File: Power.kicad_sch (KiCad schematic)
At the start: 56 parts, among them J2 Charge, J3 Battery, Q1 AO3401A, Q2 AO3400A, Q3 AO3401A, U4 FUSB303BTMX, U5 TPS61089, U6 D3V3XA4B10LP, U7 BQ25895RTW, U8 TPS63001

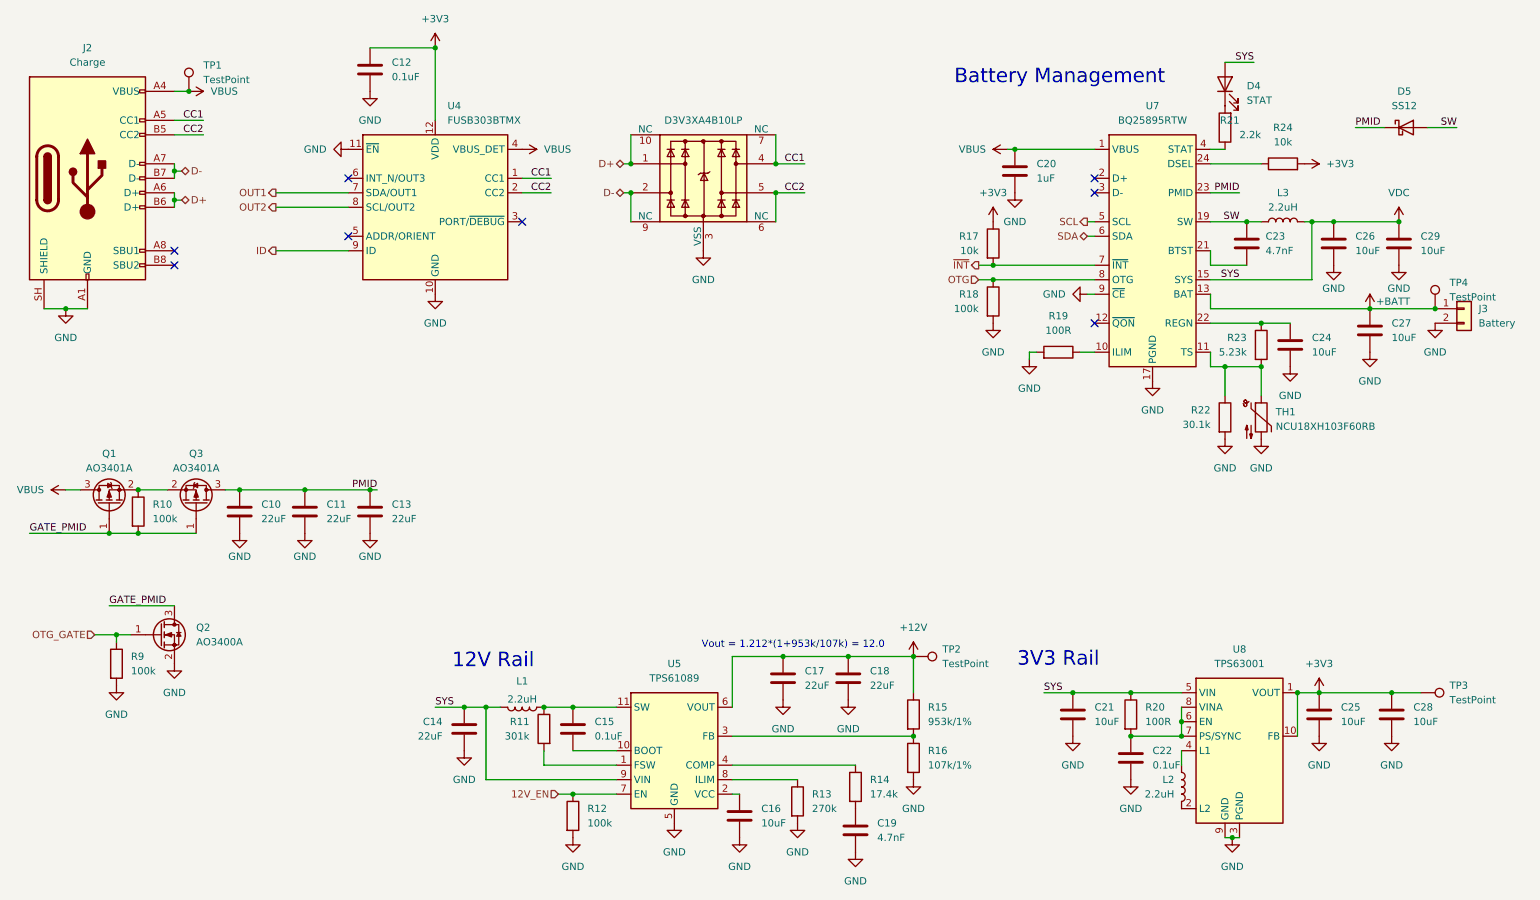
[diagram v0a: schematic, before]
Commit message: Finalize routed Cryobelt PCB for fabrication
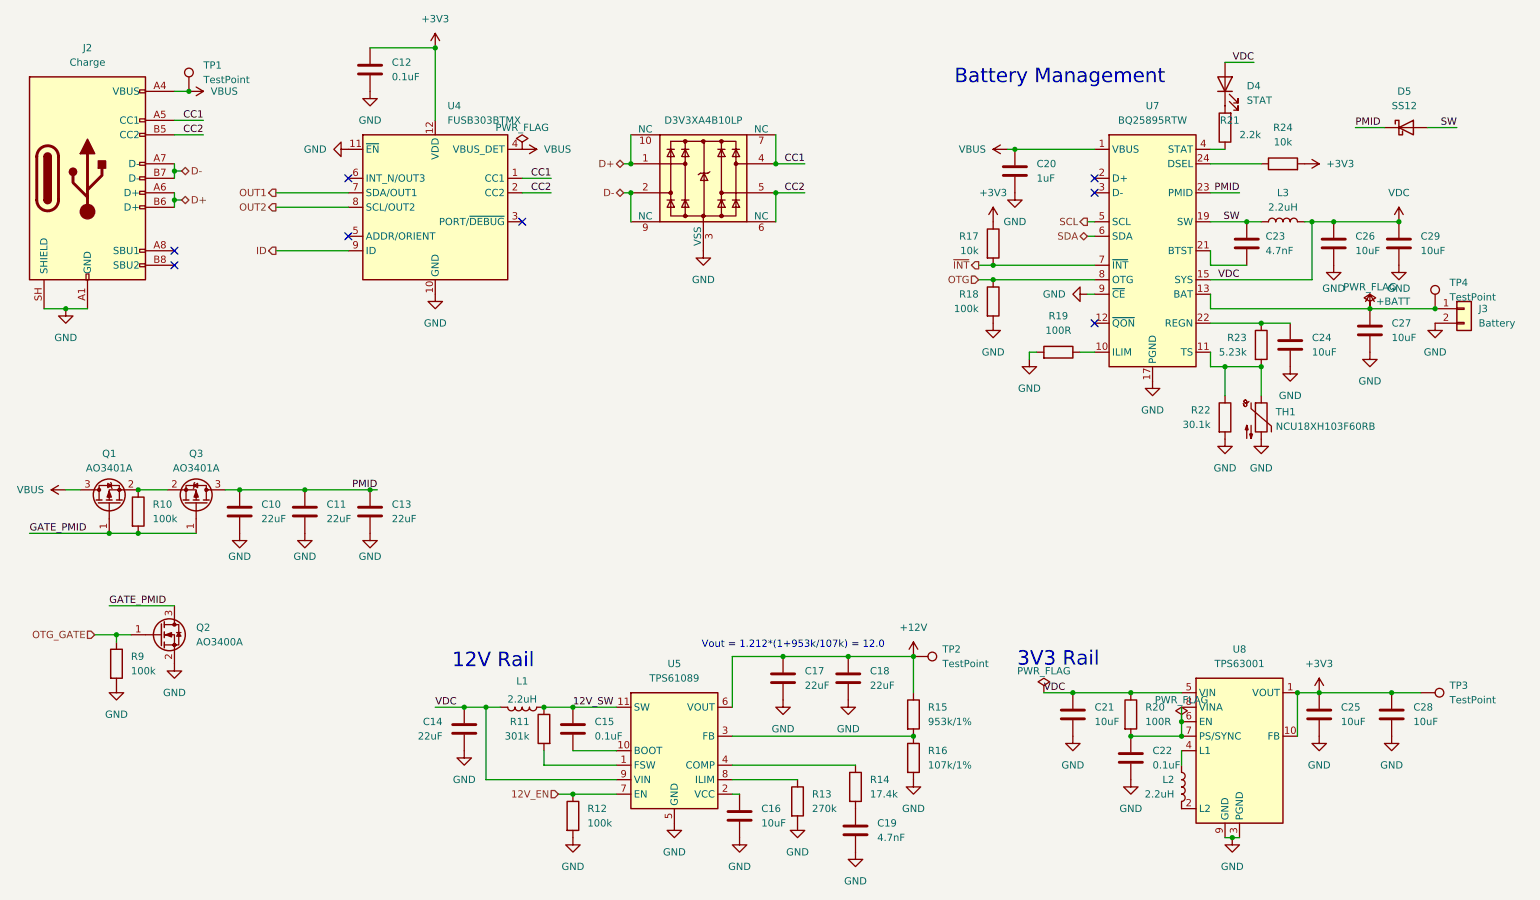
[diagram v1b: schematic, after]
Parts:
- C10, C11, C13, C17, C18: footprint Capacitor_SMD:C_0603_1608Metric -> Capacitor_SMD:C_0805_2012Metric; LCSC Part # (none) -> C20416420; MPN (none) -> TCC0805X5R226M250FT; Manufacturer (none) -> CCTC
- C12, C15, C22: LCSC Part # (none) -> C14663; MPN (none) -> CC0603KRX7R9BB104; Manufacturer (none) -> YAGEO
- C14: LCSC Part # (none) -> C86295; MPN (none) -> CL10A226MP8NUNE; Manufacturer (none) -> Samsung Electro-Mechanics
- C16, C21, C24, C25, C26, C27, C28, C29: LCSC Part # (none) -> C703114; MPN (none) -> GRM188R61A106KAALD; Manufacturer (none) -> Murata
- C19, C23: LCSC Part # (none) -> C106218; MPN (none) -> CC0603KRX7R9BB472; Manufacturer (none) -> YAGEO
- C20: LCSC Part # (none) -> C86012; MPN (none) -> GRM188R61A105KA61D; Manufacturer (none) -> Murata
- D4: LCSC Part # (none) -> C2286; MPN (none) -> KT-0603R; Manufacturer (none) -> Hubei KENTO Elec
- D5: LCSC Part # (none) -> C184027; MPN (none) -> SS12; Manufacturer (none) -> onsemi
- J2: LCSC Part # (none) -> C5143397; MPN (none) -> USB4110-GF-A; Manufacturer (none) -> Global Connector Technology
- J3: footprint Connector_Wire:SolderWire-0.5sqmm_1x02_P4.6mm_D0.9mm_OD2.1mm -> Connector_JST:JST_PH_S2B-PH-K_1x02_P2.00mm_Horizontal; LCSC Part # (none) -> C173752; MPN (none) -> S2B-PH-K-S(LF)(SN); Manufacturer (none) -> JST
- L1, L3: footprint Inductor_SMD:L_APV_ANR4020 -> Cryobelt:FEXU0420; LCSC Part # (none) -> C54777963; MPN (none) -> FEXU0420S2R2MBS; Manufacturer (none) -> cjiang
- L2: LCSC Part # (none) -> C135262; MPN (none) -> SMNR4020-2.2UH; Manufacturer (none) -> Shun Xiang Nuo
- Q1, Q3: LCSC Part # (none) -> C15127; MPN (none) -> AO3401A; Manufacturer (none) -> Alpha & Omega Semiconductor
- Q2: LCSC Part # (none) -> C20917; MPN (none) -> AO3400A; Manufacturer (none) -> Alpha & Omega Semiconductor
- R10, R12, R9: LCSC Part # (none) -> C14675; MPN (none) -> RC0603FR-07100KL; Manufacturer (none) -> YAGEO
- R11: LCSC Part # (none) -> C273742; MPN (none) -> RC0603FR-07301KL; Manufacturer (none) -> YAGEO
- R13: LCSC Part # (none) -> C137755; MPN (none) -> RC0603FR-07270KL; Manufacturer (none) -> YAGEO
- R14: LCSC Part # (none) -> C185365; MPN (none) -> RC0603FR-0717K4L; Manufacturer (none) -> YAGEO
- R15: LCSC Part # (none) -> C137669; MPN (none) -> RC0603FR-07953KL; Manufacturer (none) -> YAGEO
- R16: LCSC Part # (none) -> C245894; MPN (none) -> RC0603FR-07107KL; Manufacturer (none) -> YAGEO
- R17: symbol ScottoKeebs:Placeholder_Resistor -> Cryobelt:Placeholder_Resistor; LCSC Part # (none) -> C98220; MPN (none) -> RC0603FR-0710KL; Manufacturer (none) -> YAGEO
- R18: symbol ScottoKeebs:Placeholder_Resistor -> Cryobelt:Placeholder_Resistor; LCSC Part # (none) -> C14675; MPN (none) -> RC0603FR-07100KL; Manufacturer (none) -> YAGEO
- R19, R20: LCSC Part # (none) -> C22775; MPN (none) -> 0603WAF1000T5E; Manufacturer (none) -> UNI-ROYAL
- R21: LCSC Part # (none) -> C4190; MPN (none) -> 0603WAF2201T5E; Manufacturer (none) -> UNI-ROYAL
- R22: symbol ScottoKeebs:Placeholder_Resistor -> Cryobelt:Placeholder_Resistor; LCSC Part # (none) -> C137745; MPN (none) -> RC0603FR-0730K1L; Manufacturer (none) -> YAGEO
- R23: symbol ScottoKeebs:Placeholder_Resistor -> Cryobelt:Placeholder_Resistor; LCSC Part # (none) -> C185317; MPN (none) -> RC0603FR-075K23L; Manufacturer (none) -> YAGEO
- R24: LCSC Part # (none) -> C98220; MPN (none) -> RC0603FR-0710KL; Manufacturer (none) -> YAGEO
- TH1: LCSC Part # (none) -> C440252; MPN (none) -> NCU18XH103F60RB; Manufacturer (none) -> Murata
- U4: LCSC Part # (none) -> C895444; MPN (none) -> FUSB303BTMX; Manufacturer (none) -> onsemi
- U5: LCSC Part # (none) -> C165129; MPN (none) -> TPS61089RNRR; Manufacturer (none) -> Texas Instruments
- U6: LCSC Part # (none) -> C1980462; MPN (none) -> D3V3XA4B10LP-7; Manufacturer (none) -> Diodes Incorporated
- U7: footprint Package_DFN_QFN:Texas_RTW_WQFN-24-1EP_4x4mm_P0.5mm_EP2.7x2.7mm_ThermalVias -> Cryobelt:Texas_RTW_WQFN-24-1EP_4x4mm_P0.5mm_EP2.7x2.7mm_ThermalVias; symbol Battery_Management:BQ25895RTW -> Cryobelt_Power:BQ25895RTW; LCSC Part # (none) -> C80200; MPN (none) -> BQ25895RTWR; Manufacturer (none) -> Texas Instruments
- U8: LCSC Part # (none) -> C28060; MPN (none) -> TPS63001DRCR; Manufacturer (none) -> Texas Instruments
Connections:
- net 12V_SW: now reaches C15.1, L1.2, R11.1, U5.11 (SW)

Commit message: Resolve R15 and R25 assembly sourcing
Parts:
- R15: LCSC Part # C137669 -> C403405; MPN RC0603FR-07953KL -> ERJ3EKF9533V; Manufacturer YAGEO -> PANASONIC
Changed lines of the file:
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@@
 			)
 		)
-		(property "Manufacturer" "YAGEO"
+		(property "Manufacturer" "PANASONIC"
 			(at 0 0 0)
 			(hide yes)
@@
 			)
 		)
-		(property "MPN" "RC0603FR-07953KL"
+		(property "MPN" "ERJ3EKF9533V"
 			(at 0 0 0)
 			(hide yes)
@@
 			)
 		)
-		(property "LCSC Part #" "C137669"
+		(property "LCSC Part #" "C403405"
 			(at 0 0 0)
 			(hide yes)

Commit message: Correct charger bootstrap and audio mode values
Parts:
- C23: value 4.7nF -> 47nF; LCSC Part # C106218 -> C53084515; MPN CC0603KRX7R9BB472 -> CC0603X7R50V473KN; Manufacturer YAGEO -> TORCH
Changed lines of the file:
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@@
 			)
 		)
-		(property "Value" "4.7nF"
+		(property "Value" "47nF"
 			(at 238.252 52.07 0)
 			(show_name no)
@@
 			)
 		)
-		(property "Datasheet" ""
+		(property "Datasheet" "https://www.lcsc.com/product-detail/C53084515.html"
 			(at 234.95 50.8 0)
 			(hide yes)
@@
 			)
 		)
-		(property "Description" "Unpolarized capacitor"
+		(property "Description" "47 nF 50 V X7R bootstrap capacitor"
 			(at 234.95 50.8 0)
 			(hide yes)
@@
 			)
 		)
-		(property "Manufacturer" "YAGEO"
+		(property "Manufacturer" "TORCH"
 			(at 0 0 0)
 			(hide yes)
@@
 			)
 		)
-		(property "MPN" "CC0603KRX7R9BB472"
+		(property "MPN" "CC0603X7R50V473KN"
 			(at 0 0 0)
 			(hide yes)
@@
 			)
 		)
-		(property "LCSC Part #" "C106218"
+		(property "LCSC Part #" "C53084515"
 			(at 0 0 0)
 			(hide yes)

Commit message: Optimise BOM
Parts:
- C10, C11, C13, C17, C18: LCSC Part # C20416420 -> C45783; MPN TCC0805X5R226M250FT -> CL21A226MAQNNNE; Manufacturer CCTC -> Samsung Electro-Mechanics
- C16, C21, C24, C25, C26, C27, C28, C29: LCSC Part # C703114 -> C19702; MPN GRM188R61A106KAALD -> CL10A106KP8NNNC; Manufacturer Murata -> Samsung Electro-Mechanics
- C20: LCSC Part # C86012 -> C15849; MPN GRM188R61A105KA61D -> CL10A105KB8NNNC; Manufacturer Murata -> Samsung Electro-Mechanics
- R10, R12, R18, R9: LCSC Part # C14675 -> C25803; MPN RC0603FR-07100KL -> 0603WAF1003T5E; Manufacturer YAGEO -> UNI-ROYAL
- R17, R24: LCSC Part # C98220 -> C25804; MPN RC0603FR-0710KL -> 0603WAF1002T5E; Manufacturer YAGEO -> UNI-ROYAL
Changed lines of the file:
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@@
 			)
 		)
-		(property "Manufacturer" "Murata"
+ (property "Manufacturer" "Samsung Electro-Mechanics"
 			(at 0 0 0)
 			(hide yes)
@@
 			)
 		)
-		(property "MPN" "GRM188R61A106KAALD"
+		(property "MPN" "CL10A106KP8NNNC"
 			(at 0 0 0)
 			(hide yes)
@@
 			)
 		)
-		(property "LCSC Part #" "C703114"
+		(property "LCSC Part #" "C19702"
 			(at 0 0 0)
 			(hide yes)
@@
 			)
 		)
-		(property "Manufacturer" "CCTC"
+ (property "Manufacturer" "Samsung Electro-Mechanics"
 			(at 0 0 0)
 			(hide yes)
@@
 			)
 		)
-		(property "MPN" "TCC0805X5R226M250FT"
+		(property "MPN" "CL21A226MAQNNNE"
 			(at 0 0 0)
 			(hide yes)
@@
 			)
 		)
-		(property "LCSC Part #" "C20416420"
+		(property "LCSC Part #" "C45783"
 			(at 0 0 0)
 			(hide yes)
@@
 			)
 		)
-		(property "Manufacturer" "Murata"
+ (property "Manufacturer" "Samsung Electro-Mechanics"
 			(at 0 0 0)
 			(hide yes)
@@
 			)
 		)
-		(property "MPN" "GRM188R61A106KAALD"
+		(property "MPN" "CL10A106KP8NNNC"
 			(at 0 0 0)
 			(hide yes)
@@
 			)
 		)
-		(property "LCSC Part #" "C703114"
+		(property "LCSC Part #" "C19702"
 			(at 0 0 0)
 			(hide yes)
@@
 			)
 		)
-		(property "Manufacturer" "YAGEO"
+ (property "Manufacturer" "UNI-ROYAL"
 			(at 0 0 0)
 			(hide yes)
@@
 			)
 		)
-		(property "MPN" "RC0603FR-0710KL"
+		(property "MPN" "0603WAF1002T5E"
 			(at 0 0 0)
 			(hide yes)
@@
 			)
 		)
-		(property "LCSC Part #" "C98220"
+		(property "LCSC Part #" "C25804"
 			(at 0 0 0)
 			(hide yes)
@@
 			)
 		)
-		(property "Manufacturer" "Murata"
+ (property "Manufacturer" "Samsung Electro-Mechanics"
 			(at 0 0 0)
 			(hide yes)
@@
 			)
 		)
-		(property "MPN" "GRM188R61A106KAALD"
+		(property "MPN" "CL10A106KP8NNNC"
 			(at 0 0 0)
 			(hide yes)
@@
 			)
 		)
-		(property "LCSC Part #" "C703114"
+		(property "LCSC Part #" "C19702"
 			(at 0 0 0)
 			(hide yes)
@@
 			)
 		)
-		(property "Manufacturer" "YAGEO"
+ (property "Manufacturer" "UNI-ROYAL"
 			(at 0 0 0)
 			(hide yes)
@@
 			)
 		)
-		(property "MPN" "RC0603FR-0710KL"
+		(property "MPN" "0603WAF1002T5E"
 			(at 0 0 0)
 			(hide yes)
@@
 			)
 		)
-		(property "LCSC Part #" "C98220"
+		(property "LCSC Part #" "C25804"
 			(at 0 0 0)
 			(hide yes)
@@
 			)
 		)
-		(property "Manufacturer" "Murata"
+ (property "Manufacturer" "Samsung Electro-Mechanics"
 			(at 0 0 0)
 			(hide yes)
@@
 			)
 		)
-		(property "MPN" "GRM188R61A106KAALD"
+		(property "MPN" "CL10A106KP8NNNC"
 			(at 0 0 0)
 			(hide yes)
@@
 			)
 		)
-		(property "LCSC Part #" "C703114"
+		(property "LCSC Part #" "C19702"
 			(at 0 0 0)
 			(hide yes)
@@
 			)
 		)
-		(property "Manufacturer" "CCTC"
+ (property "Manufacturer" "Samsung Electro-Mechanics"
 			(at 0 0 0)
 			(hide yes)
@@
 			)
 		)
-		(property "MPN" "TCC0805X5R226M250FT"
+		(property "MPN" "CL21A226MAQNNNE"
 			(at 0 0 0)
 			(hide yes)
@@
 			)
 		)
-		(property "LCSC Part #" "C20416420"
+		(property "LCSC Part #" "C45783"
 			(at 0 0 0)
 			(hide yes)
@@
 			)
 		)
-		(property "Manufacturer" "CCTC"
+ (property "Manufacturer" "Samsung Electro-Mechanics"
 			(at 0 0 0)
 			(hide yes)
@@
 			)
 		)
-		(property "MPN" "TCC0805X5R226M250FT"
+		(property "MPN" "CL21A226MAQNNNE"
 			(at 0 0 0)
 			(hide yes)
@@
 			)
 		)
-		(property "LCSC Part #" "C20416420"
+		(property "LCSC Part #" "C45783"
 			(at 0 0 0)
 			(hide yes)
@@
 			)
 		)
-		(property "Manufacturer" "Murata"
+ (property "Manufacturer" "Samsung Electro-Mechanics"
 			(at 0 0 0)
 			(hide yes)
@@
 			)
 		)
-		(property "MPN" "GRM188R61A106KAALD"
+		(property "MPN" "CL10A106KP8NNNC"
 			(at 0 0 0)
 			(hide yes)
@@
 			)
 		)
-		(property "LCSC Part #" "C703114"
+		(property "LCSC Part #" "C19702"
 			(at 0 0 0)
 			(hide yes)
@@
 			)
 		)
-		(property "Manufacturer" "CCTC"
+ (property "Manufacturer" "Samsung Electro-Mechanics"
 			(at 0 0 0)
 			(hide yes)
@@
 			)
 		)
-		(property "MPN" "TCC0805X5R226M250FT"
+		(property "MPN" "CL21A226MAQNNNE"
 			(at 0 0 0)
 			(hide yes)
@@
 			)
 		)
-		(property "LCSC Part #" "C20416420"
+		(property "LCSC Part #" "C45783"
 			(at 0 0 0)
 			(hide yes)
@@
 			)
 		)
-		(property "Manufacturer" "YAGEO"
+ (property "Manufacturer" "UNI-ROYAL"
 			(at 0 0 0)
 			(hide yes)
@@
 			)
 		)
-		(property "MPN" "RC0603FR-07100KL"
+		(property "MPN" "0603WAF1003T5E"
 			(at 0 0 0)
 			(hide yes)
@@
 			)
 		)
-		(property "LCSC Part #" "C14675"
+		(property "LCSC Part #" "C25803"
 			(at 0 0 0)
 			(hide yes)
@@
 			)
 		)
-		(property "Manufacturer" "Murata"
+ (property "Manufacturer" "Samsung Electro-Mechanics"
 			(at 0 0 0)
 			(hide yes)
@@
 			)
 		)
-		(property "MPN" "GRM188R61A106KAALD"
+		(property "MPN" "CL10A106KP8NNNC"
 			(at 0 0 0)
 			(hide yes)
@@
 			)
 		)
-		(property "LCSC Part #" "C703114"
+		(property "LCSC Part #" "C19702"
 			(at 0 0 0)
 			(hide yes)
@@
 			)
 		)
-		(property "Manufacturer" "Murata"
+ (property "Manufacturer" "Samsung Electro-Mechanics"
 			(at 0 0 0)
 			(hide yes)
@@
 			)
 		)
-		(property "MPN" "GRM188R61A105KA61D"
+		(property "MPN" "CL10A105KB8NNNC"
 			(at 0 0 0)
 			(hide yes)
@@
 			)
 		)
-		(property "LCSC Part #" "C86012"
+		(property "LCSC Part #" "C15849"
 			(at 0 0 0)
 			(hide yes)
@@
 			)
 		)
-		(property "Manufacturer" "YAGEO"
+ (property "Manufacturer" "UNI-ROYAL"
 			(at 0 0 0)
 			(hide yes)
@@
 			)
 		)
-		(property "MPN" "RC0603FR-07100KL"
+		(property "MPN" "0603WAF1003T5E"
 			(at 0 0 0)
 			(hide yes)
@@
 			)
 		)
-		(property "LCSC Part #" "C14675"
+		(property "LCSC Part #" "C25803"
 			(at 0 0 0)
 			(hide yes)
@@
 			)
 		)
-		(property "Manufacturer" "YAGEO"
+ (property "Manufacturer" "UNI-ROYAL"
 			(at 0 0 0)
 			(hide yes)
@@
 			)
 		)
-		(property "MPN" "RC0603FR-07100KL"
+		(property "MPN" "0603WAF1003T5E"
 			(at 0 0 0)
 			(hide yes)
@@
 			)
 		)
-		(property "LCSC Part #" "C14675"
+		(property "LCSC Part #" "C25803"
 			(at 0 0 0)
 			(hide yes)
@@
 			)
 		)
-		(property "Manufacturer" "CCTC"
+ (property "Manufacturer" "Samsung Electro-Mechanics"
 			(at 0 0 0)
 			(hide yes)
@@
 			)
 		)
-		(property "MPN" "TCC0805X5R226M250FT"
+		(property "MPN" "CL21A226MAQNNNE"
 			(at 0 0 0)
 			(hide yes)
@@
 			)
 		)
-		(property "LCSC Part #" "C20416420"
+		(property "LCSC Part #" "C45783"
 			(at 0 0 0)
 			(hide yes)
@@
 			)
 		)
-		(property "Manufacturer" "Murata"
+ (property "Manufacturer" "Samsung Electro-Mechanics"
 			(at 0 0 0)
 			(hide yes)
@@
 			)
 		)
-		(property "MPN" "GRM188R61A106KAALD"
+		(property "MPN" "CL10A106KP8NNNC"
 			(at 0 0 0)
 			(hide yes)
@@
 			)
 		)
-		(property "LCSC Part #" "C703114"
+		(property "LCSC Part #" "C19702"
 			(at 0 0 0)
 			(hide yes)
@@
 			)
 		)
-		(property "Manufacturer" "YAGEO"
+ (property "Manufacturer" "UNI-ROYAL"
 			(at 0 0 0)
 			(hide yes)
@@
 			)
 		)
-		(property "MPN" "RC0603FR-07100KL"
+		(property "MPN" "0603WAF1003T5E"
 			(at 0 0 0)
 			(hide yes)
@@
 			)
 		)
-		(property "LCSC Part #" "C14675"
+		(property "LCSC Part #" "C25803"
 			(at 0 0 0)
 			(hide yes)
@@
 			)
 		)
-		(property "Manufacturer" "Murata"
+ (property "Manufacturer" "Samsung Electro-Mechanics"
 			(at 0 0 0)
 			(hide yes)
@@
 			)
 		)
-		(property "MPN" "GRM188R61A106KAALD"
+		(property "MPN" "CL10A106KP8NNNC"
 			(at 0 0 0)
 			(hide yes)
@@
 			)
 		)
-		(property "LCSC Part #" "C703114"
+		(property "LCSC Part #" "C19702"
 			(at 0 0 0)
 			(hide yes)

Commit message: Optimise BOM
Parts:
- C19: LCSC Part # C106218 -> C53987; MPN CC0603KRX7R9BB472 -> 0603B472K500NT
- C23: LCSC Part # C53084515 -> C1622; MPN CC0603X7R50V473KN -> CL10B473KB8NNNC; Manufacturer TORCH -> Samsung Electro-Mechanics
- R11: value 301k -> 300k; LCSC Part # C273742 -> C23024; MPN RC0603FR-07301KL -> 0603WAF3003T5E
- R13: value 270k -> 300k; LCSC Part # C137755 -> C23024; MPN RC0603FR-07270KL -> 0603WAF3003T5E
- R22: value 30.1k -> 30k; MPN RC0603FR-0730K1L -> 0603WAF3002T5E
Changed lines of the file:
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@@
 			)
 		)
-		(property "Value" "30.1k"
+		(property "Value" "30k"
 			(at 228.6 82.5499 90)
 			(show_name no)
@@
 			)
 		)
-		(property "MPN" "RC0603FR-0730K1L"
+		(property "MPN" "0603WAF3002T5E"
 			(at 0 0 0)
 			(hide yes)
@@
 			)
 		)
-		(property "Value" "270k"
+		(property "Value" "300k"
 			(at 158.75 149.8599 0)
 			(show_name no)
@@
 			)
 		)
-		(property "MPN" "RC0603FR-07270KL"
+		(property "MPN" "0603WAF3003T5E"
 			(at 0 0 0)
 			(hide yes)
@@
 			)
 		)
-		(property "LCSC Part #" "C137755"
+		(property "LCSC Part #" "C23024"
 			(at 0 0 0)
 			(hide yes)
@@
 			)
 		)
-		(property "Manufacturer" "TORCH"
+		(property "Manufacturer" "Samsung Electro-Mechanics"
 			(at 0 0 0)
 			(hide yes)
@@
 			)
 		)
-		(property "MPN" "CC0603X7R50V473KN"
+		(property "MPN" "CL10B473KB8NNNC"
 			(at 0 0 0)
 			(hide yes)
@@
 			)
 		)
-		(property "LCSC Part #" "C53084515"
+		(property "LCSC Part #" "C1622"
 			(at 0 0 0)
 			(hide yes)
@@
 			)
 		)
-		(property "MPN" "CC0603KRX7R9BB472"
+		(property "MPN" "0603B472K500NT"
 			(at 0 0 0)
 			(hide yes)
@@
 			)
 		)
-		(property "LCSC Part #" "C106218"
+		(property "LCSC Part #" "C53987"
 			(at 0 0 0)
 			(hide yes)
@@
 			)
 		)
-		(property "Value" "301k"
+		(property "Value" "300k"
 			(at 109.22 137.1599 0)
 			(show_name no)
@@
 			)
 		)
-		(property "MPN" "RC0603FR-07301KL"
+		(property "MPN" "0603WAF3003T5E"
 			(at 0 0 0)
 			(hide yes)
@@
 			)
 		)
-		(property "LCSC Part #" "C273742"
+		(property "LCSC Part #" "C23024"
 			(at 0 0 0)
 			(hide yes)
